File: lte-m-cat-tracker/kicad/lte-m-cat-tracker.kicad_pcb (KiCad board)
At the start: 2 copper layers, 30 x 35 mm, 33 parts, among them J1 JST-GH-1.25mm-2P, J2 USB-C-16P, SW1 MSK12C02, U1 SIM7080G-M, U2 ESP32-C3, U3 LIS2DW12TR, U4 TP4056, U5 XC6220B331MR-G

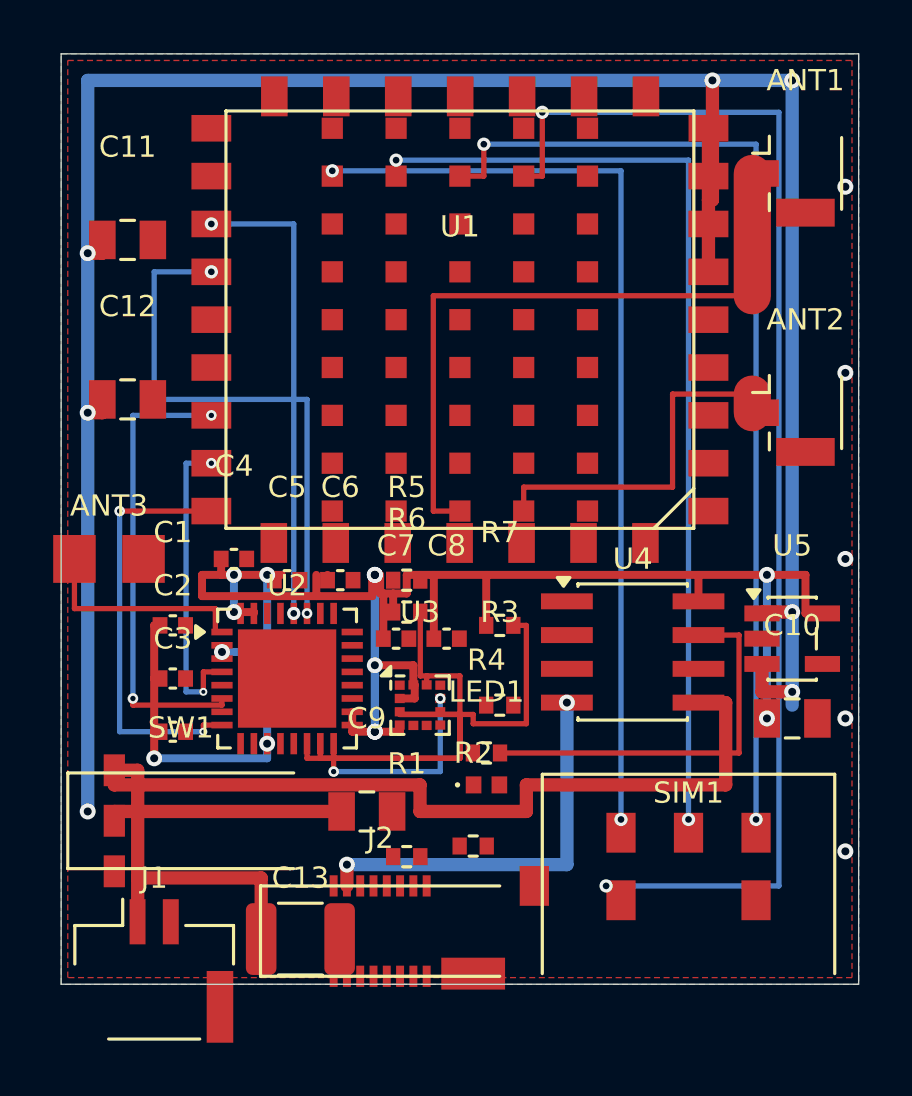
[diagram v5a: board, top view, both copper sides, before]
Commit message: fix_crossings_v4: crossing修正試み（shorts/crossing残存・作業継続中）
- fix_crossings_v3.py: 新セグメントがkicad_pcb閉じ括弧外に出るバグあり（無効）
- fix_crossings_v4.py: 挿入位置を修正(closing)前に変更
  - Fix1: SIM_RESETN横→B.Cu（+3.3V縦x=3.5回避）
  - Fix2: I2C_SDA→y=27.2+x=16.0迂回（SCL共有解消）
  - Fix3: VBAT縦→F.Cu x=1.5迂回（VBAT_SW横y=28.5回避）
  - Fix4: CHRG縦x=24.3（VBAT縦x=25.0回避）
  - Fix5: SIM_RXD S字迂回x=9.75
  - Fix6: ACCEL_INT1→B.Cu縦（SCL横y=26.5回避）
- 現状: shorts=11, crossing=3, 未配線=39（元と同数・断線なし）
- 次: shorts/crossingの根本原因（座標ミス）を修正

Co-Authored-By: Claude Sonnet 4.6 <noreply@anthropic.com>
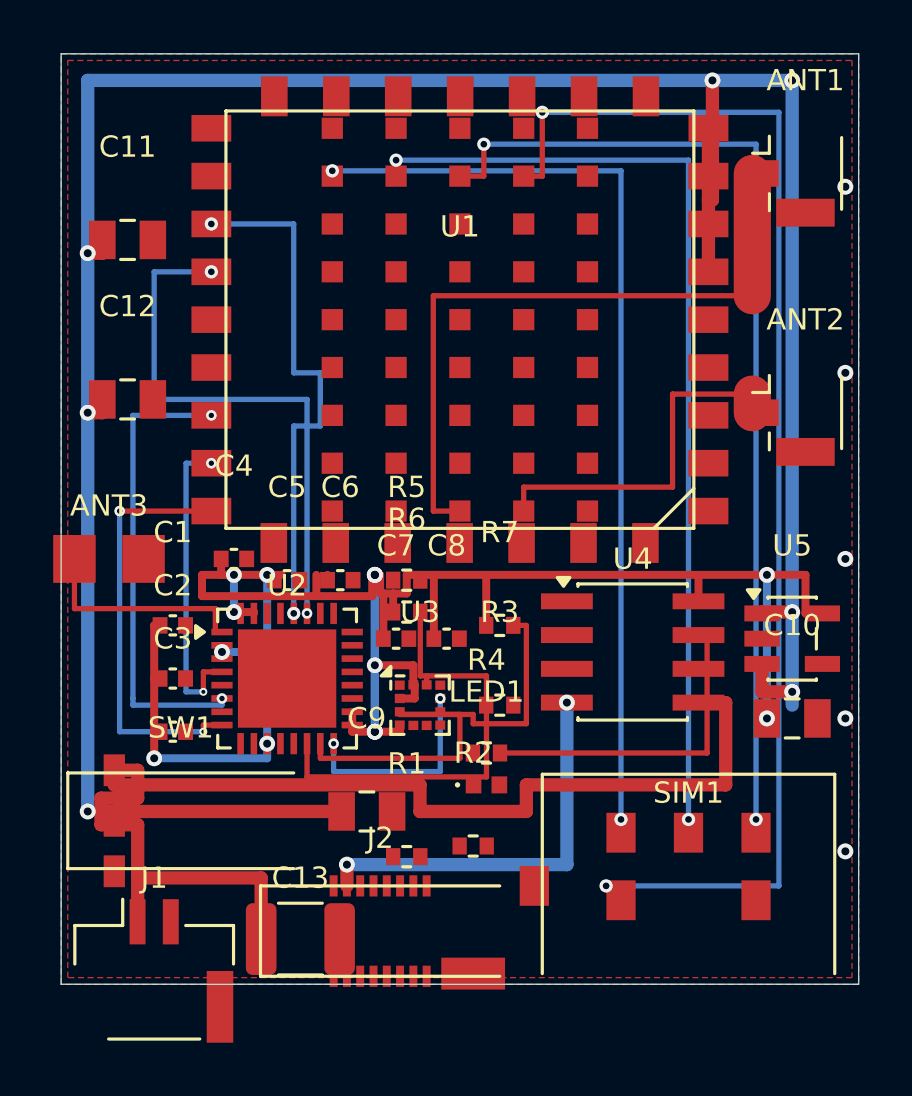
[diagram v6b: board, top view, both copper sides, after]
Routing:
- net I2C_SDA: track 13.6 -> 17.0 mm
- net VBAT: track 43.2 -> 46.0 mm
- net CHRG: track 14.9 -> 12.6 mm
- net SIM_RXD: track 17.8 -> 19.8 mm
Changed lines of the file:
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@@
 	(via (at 29.5 25.0) (size 0.6) (drill 0.3) (layers "F.Cu" "B.Cu") (net "GND"))
 	(via (at 29.5 30.0) (size 0.6) (drill 0.3) (layers "F.Cu" "B.Cu") (net "GND"))
-	(segment (start 2.88 32.65) (end 2.88 26.95) (width 0.5) (layer "F.Cu") (net "VBAT"))
 	(segment (start 2.88 26.95) (end 2.0 26.95) (width 0.5) (layer "F.Cu") (net "VBAT"))
 	(segment (start 2.0 26.95) (end 2.0 27.5) (width 0.5) (layer "F.Cu") (net "VBAT"))
@@
 	(segment (start 5.65 13.6) (end 2.7 13.6) (width 0.2) (layer "B.Cu") (net "SIM_RESETN"))
 	(segment (start 2.7 13.6) (end 2.7 24.25) (width 0.2) (layer "B.Cu") (net "SIM_RESETN"))
-	(via (at 2.7 24.25) (size 0.4) (drill 0.2) (layers "F.Cu" "B.Cu") (net "SIM_RESETN"))
-	(segment (start 2.7 24.25) (end 2.7 24.5) (width 0.2) (layer "F.Cu") (net "SIM_RESETN"))
-	(segment (start 2.7 24.5) (end 6.05 24.5) (width 0.2) (layer "F.Cu") (net "SIM_RESETN"))
-	(segment (start 6.05 24.5) (end 6.05 24.25) (width 0.2) (layer "F.Cu") (net "SIM_RESETN"))
+	(segment (start 2.7 24.25) (end 2.7 24.5) (width 0.2) (layer "B.Cu") (net "SIM_RESETN"))
+	(segment (start 2.7 24.5) (end 6.05 24.5) (width 0.2) (layer "B.Cu") (net "SIM_RESETN"))
+	(segment (start 6.05 24.5) (end 6.05 24.25) (width 0.2) (layer "B.Cu") (net "SIM_RESETN"))
 	(via (at 5.65 8.2) (size 0.5) (drill 0.25) (layers "F.Cu" "B.Cu") (net "SIM_TXD"))
 	(segment (start 5.65 8.2) (end 3.5 8.2) (width 0.2) (layer "B.Cu") (net "SIM_TXD"))
@@
 	(via (at 5.65 6.4) (size 0.5) (drill 0.25) (layers "F.Cu" "B.Cu") (net "SIM_RXD"))
 	(segment (start 5.65 6.4) (end 8.75 6.4) (width 0.2) (layer "B.Cu") (net "SIM_RXD"))
-	(segment (start 8.75 6.4) (end 8.75 20.0) (width 0.2) (layer "B.Cu") (net "SIM_RXD"))
 	(segment (start 10.2 4.6) (end 10.2 4.4) (width 0.2) (layer "F.Cu") (net "SIM_VDD"))
 	(via (at 10.2 4.4) (size 0.5) (drill 0.25) (layers "F.Cu" "B.Cu") (net "SIM_VDD"))
@@
 	(segment (start 17.5 25.2) (end 17.5 21.5) (width 0.2) (layer "F.Cu") (net "I2C_SCL"))
 	(segment (start 17.5 21.5) (end 17.01 21.5) (width 0.2) (layer "F.Cu") (net "I2C_SCL"))
-	(segment (start 9.25 25.95) (end 9.25 26.5) (width 0.2) (layer "F.Cu") (net "I2C_SDA"))
-	(segment (start 9.25 26.5) (end 15.0 26.5) (width 0.2) (layer "F.Cu") (net "I2C_SDA"))
-	(segment (start 15.0 26.5) (end 15.0 23.4) (width 0.2) (layer "F.Cu") (net "I2C_SDA"))
-	(segment (start 15.0 23.4) (end 13.75 23.4) (width 0.2) (layer "F.Cu") (net "I2C_SDA"))
-	(segment (start 13.75 23.4) (end 13.75 23.738) (width 0.2) (layer "F.Cu") (net "I2C_SDA"))
+					(segment (start 13.75 23.4) (end 13.75 23.738) (width 0.2) (layer "F.Cu") (net "I2C_SDA"))
 	(segment (start 13.75 23.4) (end 13.51 23.4) (width 0.2) (layer "F.Cu") (net "I2C_SDA"))
 	(segment (start 13.51 23.4) (end 13.51 21.0) (width 0.2) (layer "F.Cu") (net "I2C_SDA"))
-	(segment (start 23.975 21.865) (end 25.5 21.865) (width 0.2) (layer "F.Cu") (net "CHRG"))
-	(segment (start 25.5 21.865) (end 25.5 26.3) (width 0.2) (layer "F.Cu") (net "CHRG"))
-	(segment (start 25.5 26.3) (end 16.51 26.3) (width 0.2) (layer "F.Cu") (net "CHRG"))
-	(via (at 14.262 24.25) (size 0.4) (drill 0.2) (layers "F.Cu" "B.Cu") (net "ACCEL_INT1"))
+				(via (at 14.262 24.25) (size 0.4) (drill 0.2) (layers "F.Cu" "B.Cu") (net "ACCEL_INT1"))
 	(segment (start 14.262 24.25) (end 14.262 27.0) (width 0.2) (layer "B.Cu") (net "ACCEL_INT1"))
 	(segment (start 14.262 27.0) (end 10.25 27.0) (width 0.2) (layer "B.Cu") (net "ACCEL_INT1"))
-	(via (at 10.25 27.0) (size 0.4) (drill 0.2) (layers "F.Cu" "B.Cu") (net "ACCEL_INT1"))
-	(segment (start 10.25 27.0) (end 10.25 25.95) (width 0.2) (layer "F.Cu") (net "ACCEL_INT1"))
+	(segment (start 10.25 27.0) (end 10.25 25.95) (width 0.2) (layer "B.Cu") (net "ACCEL_INT1"))
 	(segment (start 8.75 20.0) (end 8.75 21.05) (width 0.2) (layer "B.Cu") (net "SIM_RXD"))
 	(via (at 8.75 21.05) (size 0.5) (drill 0.25) (layers "F.Cu" "B.Cu") (net "SIM_RXD"))
@@
 	)
 	(embedded_fonts no)
+	(via (at 6.05 24.25) (size 0.4) (drill 0.2) (layers "F.Cu" "B.Cu") (net "SIM_RESETN"))
+	(segment (start 9.25 25.95) (end 9.25 27.2) (width 0.2) (layer "F.Cu") (net "I2C_SDA"))
+	(segment (start 9.25 27.2) (end 16.0 27.2) (width 0.2) (layer "F.Cu") (net "I2C_SDA"))
+	(segment (start 16.0 27.2) (end 16.0 23.4) (width 0.2) (layer "F.Cu") (net "I2C_SDA"))
+	(segment (start 16.0 23.4) (end 13.75 23.4) (width 0.2) (layer "F.Cu") (net "I2C_SDA"))
+	(segment (start 2.88 32.65) (end 2.88 29.0) (width 0.5) (layer "F.Cu") (net "VBAT"))
+	(segment (start 2.88 29.0) (end 1.5 29.0) (width 0.5) (layer "F.Cu") (net "VBAT"))
+	(segment (start 1.5 29.0) (end 1.5 28.0) (width 0.5) (layer "F.Cu") (net "VBAT"))
+	(segment (start 1.5 28.0) (end 2.88 28.0) (width 0.5) (layer "F.Cu") (net "VBAT"))
+	(segment (start 2.88 28.0) (end 2.88 26.95) (width 0.5) (layer "F.Cu") (net "VBAT"))
+	(segment (start 23.975 21.865) (end 24.3 21.865) (width 0.2) (layer "F.Cu") (net "CHRG"))
+	(segment (start 24.3 21.865) (end 24.3 26.3) (width 0.2) (layer "F.Cu") (net "CHRG"))
+	(segment (start 24.3 26.3) (end 16.51 26.3) (width 0.2) (layer "F.Cu") (net "CHRG"))
+	(segment (start 8.75 6.4) (end 8.75 12.0) (width 0.2) (layer "B.Cu") (net "SIM_RXD"))
+	(segment (start 8.75 12.0) (end 9.75 12.0) (width 0.2) (layer "B.Cu") (net "SIM_RXD"))
+	(segment (start 9.75 12.0) (end 9.75 14.0) (width 0.2) (layer "B.Cu") (net "SIM_RXD"))
+	(segment (start 9.75 14.0) (end 8.75 14.0) (width 0.2) (layer "B.Cu") (net "SIM_RXD"))
+	(segment (start 8.75 14.0) (end 8.75 20.0) (width 0.2) (layer "B.Cu") (net "SIM_RXD"))
+	(via (at 10.25 25.95) (size 0.4) (drill 0.2) (layers "F.Cu" "B.Cu") (net "ACCEL_INT1"))
 )

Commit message: fix_crossings_v5: shorts=0件 crossings=0件 ✅
Fix2: I2C_SDA → y=27.0+x=13.65迂回（SCL縦/+3.3V横/CHRG横を全回避）
Fix3: VBAT J1→SW1をB.Cu縦x=2.875化（VBAT_SW F.Cu全要素を層分離で回避）
Fix4: CHRG縦x=24.3→x=22.5（VBAT pad5 left_edge=23.0からgap 0.4mm）
Fix5: SIM_RXD S字廃止+SIM_TXD x=8.3迂回y=21.45（SIM_RXD via gap 0.10mm）

Co-Authored-By: Claude Sonnet 4.6 <noreply@anthropic.com>
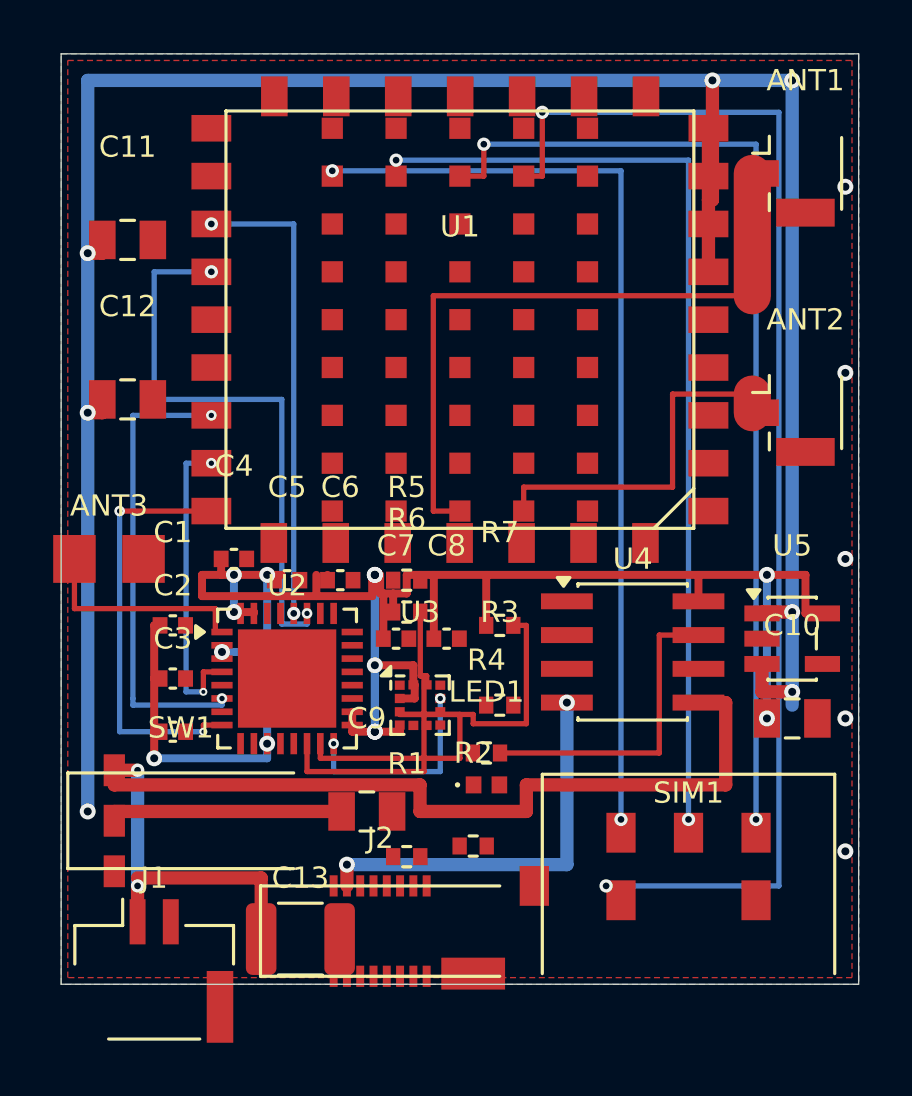
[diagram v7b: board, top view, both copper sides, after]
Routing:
- net I2C_SDA: track 17.0 -> 12.1 mm
- net VBAT: track 46.0 -> 43.2 mm, vias 0 -> 2
- net SIM_RXD: track 19.8 -> 17.8 mm
- net SIM_TXD: track 20.8 -> 21.6 mm
- net CHRG: track 12.6 -> 11.9 mm
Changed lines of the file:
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@@
 	(segment (start 5.65 8.2) (end 3.5 8.2) (width 0.2) (layer "B.Cu") (net "SIM_TXD"))
 	(segment (start 3.5 8.2) (end 3.5 13.0) (width 0.2) (layer "B.Cu") (net "SIM_TXD"))
-	(segment (start 3.5 13.0) (end 9.25 13.0) (width 0.2) (layer "B.Cu") (net "SIM_TXD"))
-	(segment (start 9.25 13.0) (end 9.25 21.05) (width 0.2) (layer "B.Cu") (net "SIM_TXD"))
-	(via (at 9.25 21.05) (size 0.4) (drill 0.2) (layers "F.Cu" "B.Cu") (net "SIM_TXD"))
+			(via (at 9.25 21.05) (size 0.4) (drill 0.2) (layers "F.Cu" "B.Cu") (net "SIM_TXD"))
 	(via (at 5.65 6.4) (size 0.5) (drill 0.25) (layers "F.Cu" "B.Cu") (net "SIM_RXD"))
 	(segment (start 5.65 6.4) (end 8.75 6.4) (width 0.2) (layer "B.Cu") (net "SIM_RXD"))
@@
 	(embedded_fonts no)
 	(via (at 6.05 24.25) (size 0.4) (drill 0.2) (layers "F.Cu" "B.Cu") (net "SIM_RESETN"))
-	(segment (start 9.25 25.95) (end 9.25 27.2) (width 0.2) (layer "F.Cu") (net "I2C_SDA"))
-	(segment (start 9.25 27.2) (end 16.0 27.2) (width 0.2) (layer "F.Cu") (net "I2C_SDA"))
-	(segment (start 16.0 27.2) (end 16.0 23.4) (width 0.2) (layer "F.Cu") (net "I2C_SDA"))
-	(segment (start 16.0 23.4) (end 13.75 23.4) (width 0.2) (layer "F.Cu") (net "I2C_SDA"))
-	(segment (start 2.88 32.65) (end 2.88 29.0) (width 0.5) (layer "F.Cu") (net "VBAT"))
-	(segment (start 2.88 29.0) (end 1.5 29.0) (width 0.5) (layer "F.Cu") (net "VBAT"))
-	(segment (start 1.5 29.0) (end 1.5 28.0) (width 0.5) (layer "F.Cu") (net "VBAT"))
-	(segment (start 1.5 28.0) (end 2.88 28.0) (width 0.5) (layer "F.Cu") (net "VBAT"))
-	(segment (start 2.88 28.0) (end 2.88 26.95) (width 0.5) (layer "F.Cu") (net "VBAT"))
-	(segment (start 23.975 21.865) (end 24.3 21.865) (width 0.2) (layer "F.Cu") (net "CHRG"))
-	(segment (start 24.3 21.865) (end 24.3 26.3) (width 0.2) (layer "F.Cu") (net "CHRG"))
-	(segment (start 24.3 26.3) (end 16.51 26.3) (width 0.2) (layer "F.Cu") (net "CHRG"))
-	(segment (start 8.75 6.4) (end 8.75 12.0) (width 0.2) (layer "B.Cu") (net "SIM_RXD"))
-	(segment (start 8.75 12.0) (end 9.75 12.0) (width 0.2) (layer "B.Cu") (net "SIM_RXD"))
-	(segment (start 9.75 12.0) (end 9.75 14.0) (width 0.2) (layer "B.Cu") (net "SIM_RXD"))
-	(segment (start 9.75 14.0) (end 8.75 14.0) (width 0.2) (layer "B.Cu") (net "SIM_RXD"))
-	(segment (start 8.75 14.0) (end 8.75 20.0) (width 0.2) (layer "B.Cu") (net "SIM_RXD"))
-	(via (at 10.25 25.95) (size 0.4) (drill 0.2) (layers "F.Cu" "B.Cu") (net "ACCEL_INT1"))
+													(via (at 10.25 25.95) (size 0.4) (drill 0.2) (layers "F.Cu" "B.Cu") (net "ACCEL_INT1"))
+	(segment (start 9.25 25.95) (end 9.25 27.0) (width 0.2) (layer "F.Cu") (net "I2C_SDA"))
+	(segment (start 9.25 27.0) (end 13.65 27.0) (width 0.2) (layer "F.Cu") (net "I2C_SDA"))
+	(segment (start 13.65 27.0) (end 13.65 23.4) (width 0.2) (layer "F.Cu") (net "I2C_SDA"))
+	(segment (start 13.65 23.4) (end 13.75 23.4) (width 0.2) (layer "F.Cu") (net "I2C_SDA"))
+	(segment (start 2.875 32.65) (end 2.875 31.3) (width 0.5) (layer "F.Cu") (net "VBAT"))
+	(via (at 2.875 31.3) (size 0.5) (drill 0.25) (layers "F.Cu" "B.Cu") (net "VBAT"))
+	(segment (start 2.875 31.3) (end 2.875 26.95) (width 0.5) (layer "B.Cu") (net "VBAT"))
+	(via (at 2.875 26.95) (size 0.5) (drill 0.25) (layers "F.Cu" "B.Cu") (net "VBAT"))
+	(segment (start 23.975 21.865) (end 22.5 21.865) (width 0.2) (layer "F.Cu") (net "CHRG"))
+	(segment (start 22.5 21.865) (end 22.5 26.3) (width 0.2) (layer "F.Cu") (net "CHRG"))
+	(segment (start 22.5 26.3) (end 16.51 26.3) (width 0.2) (layer "F.Cu") (net "CHRG"))
+	(segment (start 8.75 6.4) (end 8.75 20.0) (width 0.2) (layer "B.Cu") (net "SIM_RXD"))
+	(segment (start 3.5 13.0) (end 8.3 13.0) (width 0.2) (layer "B.Cu") (net "SIM_TXD"))
+	(segment (start 8.3 13.0) (end 8.3 21.45) (width 0.2) (layer "B.Cu") (net "SIM_TXD"))
+	(segment (start 8.3 21.45) (end 9.25 21.45) (width 0.2) (layer "B.Cu") (net "SIM_TXD"))
+	(segment (start 9.25 21.45) (end 9.25 21.05) (width 0.2) (layer "B.Cu") (net "SIM_TXD"))
 )

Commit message: PCB: VBAT_SW断線修正・GNDビア追加・ゾーン充填
- VBAT_SW F.Cu segment追加: via(1,28.5)↔SW1.pad2(2,28.5)接続
- GNDビア4本追加: (4.0,18.5),(17.5,27.5),(19.5,23.5),(25.5,11.5)
- KiCad Python APIでGNDゾーン充填実行

DRC結果: shorts=0件 ✅ crossings=0件 ✅
残りunconnected 11件は全てGNDゾーン孤島（KiCad GUIで要確認）

Co-Authored-By: Claude Sonnet 4.6 <noreply@anthropic.com>
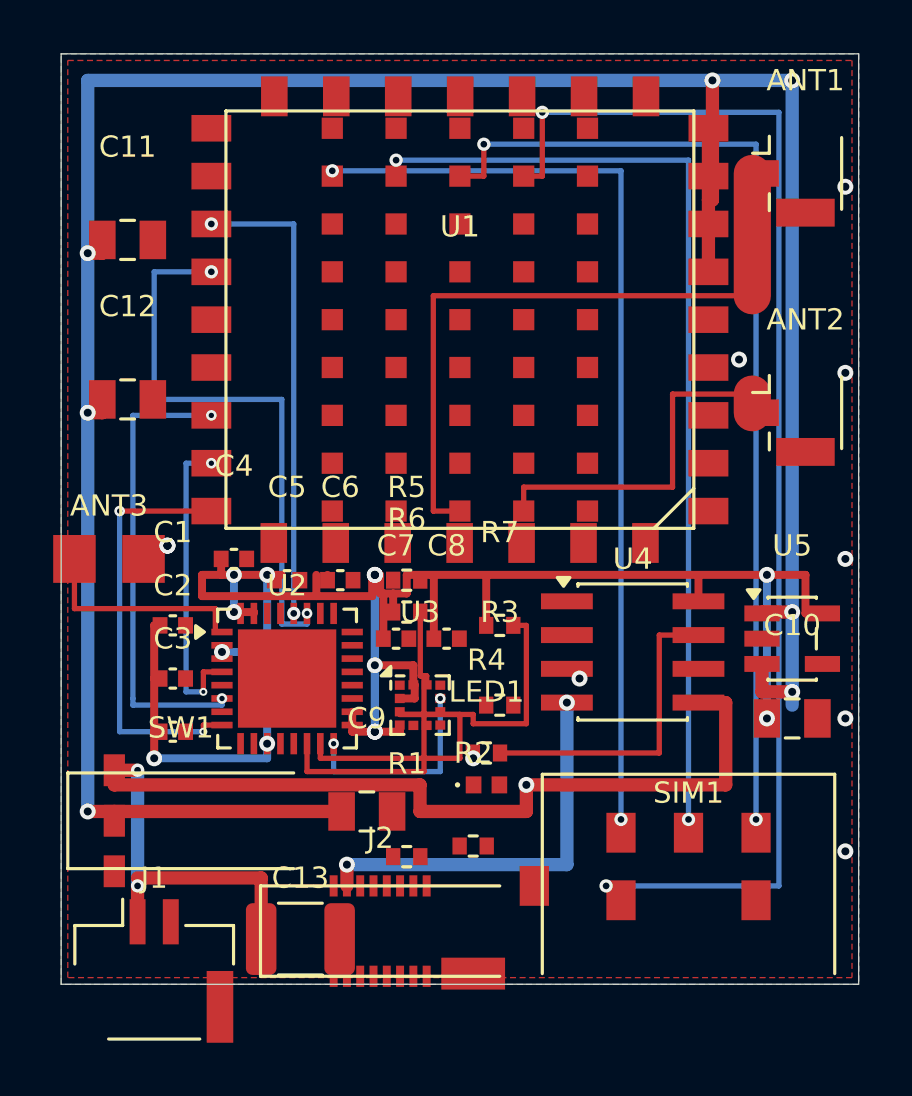
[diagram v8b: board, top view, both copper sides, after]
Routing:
- net VBAT_SW: track 101.9 -> 102.9 mm
- net VBAT: vias 2 -> 3
- net GND: vias 5 -> 10
